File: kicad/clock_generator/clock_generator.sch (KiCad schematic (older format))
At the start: 17 parts, among them J1 DB9_Male, U1 SN74ALVC00, U2 SN74ALVC00, U3 SN74ALVC00, U4 SN74ALVC00

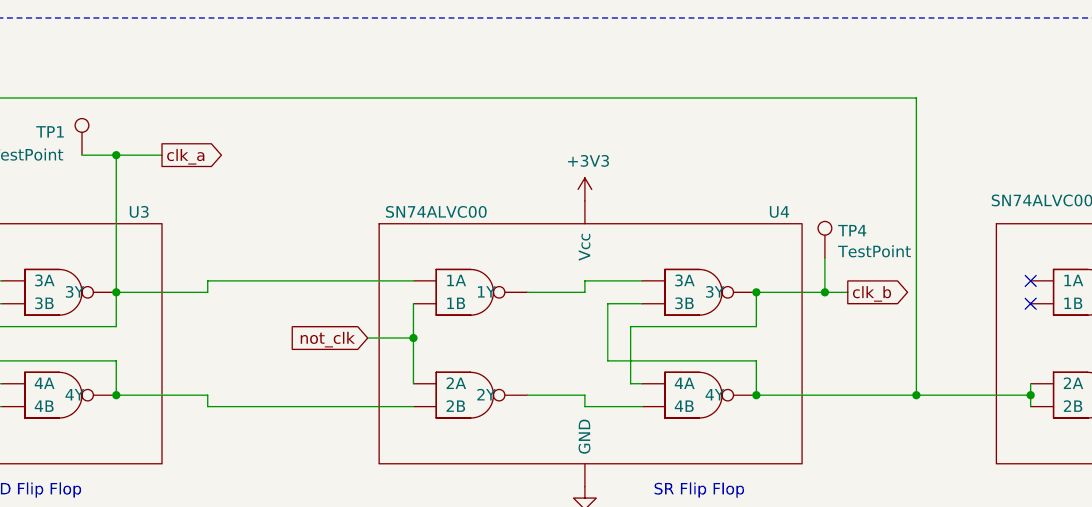
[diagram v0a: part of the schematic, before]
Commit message: Flipped clk A and clk B based on timing plan.
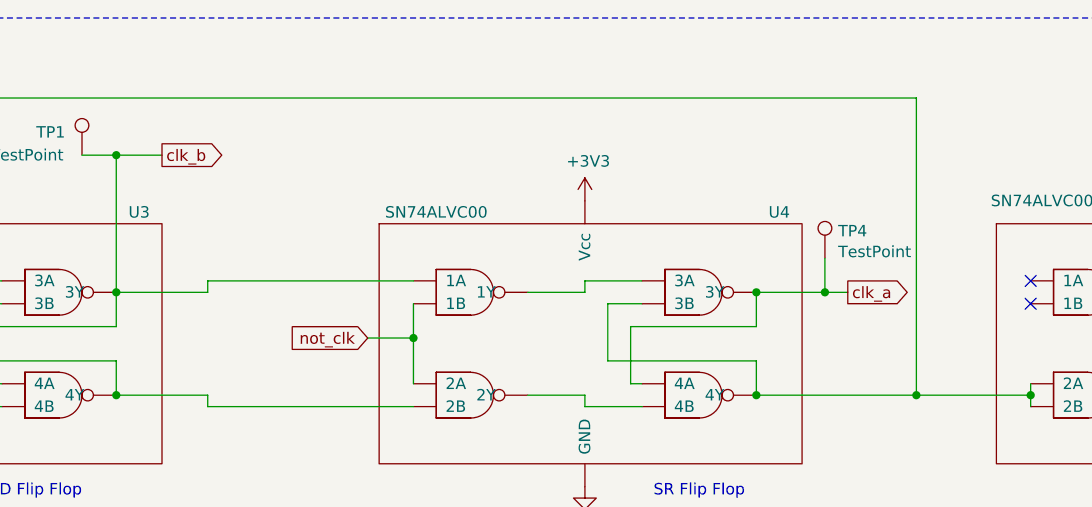
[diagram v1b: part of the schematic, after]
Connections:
- net clk_a: now also TP4.1, U4.12 (4A), U4.8 (3Y); no longer TP1.1, U3.12 (4A), U3.8 (3Y), U4.1 (1A)
- net clk_b: now also TP1.1, U3.12 (4A), U3.8 (3Y), U4.1 (1A); no longer TP4.1, U4.12 (4A), U4.8 (3Y)
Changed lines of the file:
@@
 Connection ~ 3950 2600
 Text GLabel 4150 1550 2    50   Output ~ 0
-clk_a
+clk_b
 Wire Wire Line
 	3950 2150 3950 1550
@@
 	3950 1550 4150 1550
 Text GLabel 7150 2150 2    50   Output ~ 0
-clk_b
+clk_a
 Wire Wire Line
 	3000 5600 3050 5600

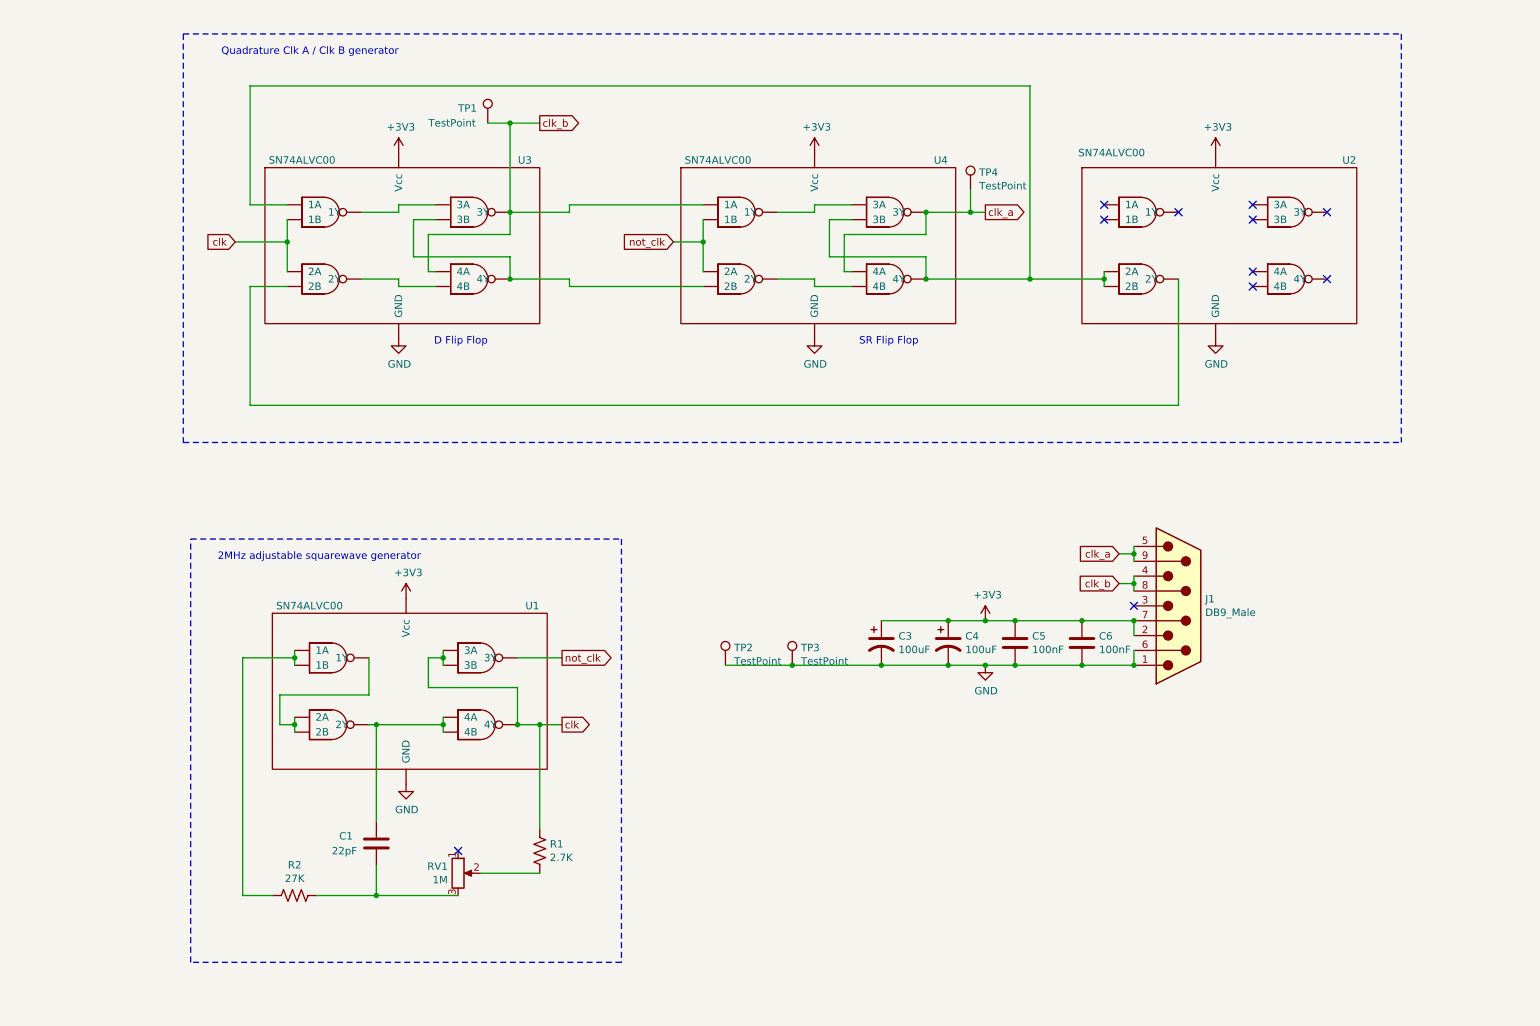
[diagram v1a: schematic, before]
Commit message: Ram (#5)
* Flipped clk A and B based on timing diagram. Added output buffers for clock signals.

* Added clock output enable signal to motherboard debugger. Updated component library.

* Schematic and layout for RAM board complete.

* ALU schematic complete, ready for layout and routing.

* ALU layout, routing complete. Associated motherboard mod. 

* Added Load LED to register and program counter boards.
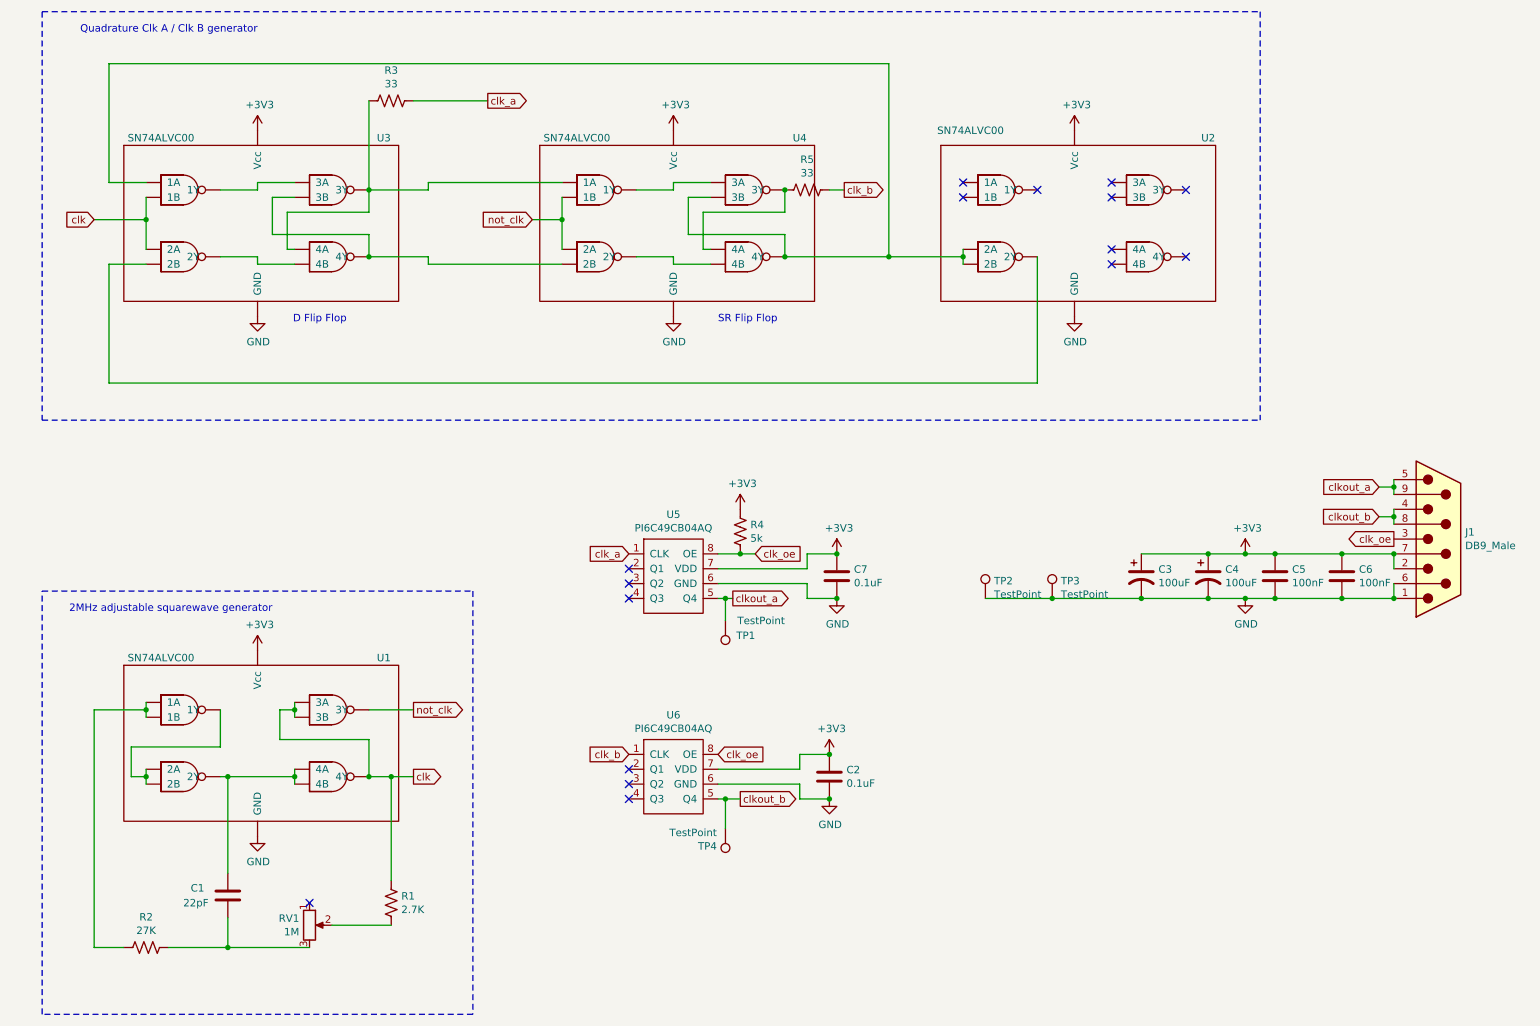
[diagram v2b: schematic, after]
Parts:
- added C2, C7: 0.1uF, Capacitor_SMD:C_1206_3216Metric, symbol Device:C
- added R3, R5: 33, Resistor_SMD:R_1206_3216Metric, symbol Device:R_US
- added R4: 5k, Resistor_SMD:R_1206_3216Metric, symbol Device:R_US
- added U5, U6: PI6C49CB04AQ, Package_SO:SOIC-8_3.9x4.9mm_P1.27mm, symbol NANDIRL_components:PI6C49CB04AQ
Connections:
- net +3V3: now also C2.1, C7.1, R4.2, U5.7 (VDD), U6.7 (VDD)
- net GND: now also C2.2, C7.2, U5.6 (GND), U6.6 (GND)
- net clk_a: now also R3.1, U5.1 (CLK); no longer J1.5, J1.9, TP4.1, U4.12 (4A), U4.8 (3Y)
- net clk_b: now also R5.1, U6.1 (CLK); no longer J1.4, J1.8, TP1.1, U3.12 (4A), U3.8 (3Y), U4.1 (1A)
- net clk_oe: now reaches J1.3
- net clk_oe: now also R4.1, U5.8 (OE), U6.8 (OE)
- new net: R3.2, U3.12 (4A), U3.8 (3Y), U4.1 (1A)
- new net: R5.2, U4.12 (4A), U4.8 (3Y)
- new net clkout_a: J1.5, J1.9, TP1.1, U5.5 (Q4)
- new net clkout_b: J1.4, J1.8, TP4.1, U6.5 (Q4)
- no-connect marks 11 -> 16
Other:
- moved on the sheet: C1, C3, C4, C5, C6, J1, R1, R2, RV1, TP1, TP2, TP3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

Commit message: Readme updates (#6)
* Readme intro section

* Board revisions for manufacturing, add digikey PNs to all, added logo.
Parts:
- C2, C7: Digikey PN (none) -> 399-C1206C104K5RAC7800CT-ND
- J1: footprint Connector_Dsub:DSUB-9_Male_Horizontal_P2.77x2.84mm_EdgePinOffset4.94mm_Housed_MountingHolesOffset7.48mm -> Connector_Dsub:DSUB-9_Male_Horizontal_P2.77x2.84mm_EdgePinOffset7.70mm_Housed_MountingHolesOffset9.12mm; Digikey PN (none) -> AE10968-ND
- R3, R5: Digikey PN (none) -> P33ECT-ND
- R4: Digikey PN (none) -> P5.1KECT-ND
- U1, U2, U3, U4: Digikey PN (none) -> 296-5104-1-ND
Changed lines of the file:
@@
 F 2 "Package_SO:TSSOP-14_4.4x5mm_P0.65mm" H 2250 -200 50  0001 C CNN
 F 3 "" H 2500 1300 50  0001 C CNN
+F 4 "296-5104-1-ND" H 0   0   50  0001 C CNN "Digikey PN"
 	1    2500 1300
 	1    0    0    -1
@@
 F 2 "Package_SO:TSSOP-14_4.4x5mm_P0.65mm" H 2250 3300 50  0001 C CNN
 F 3 "" H 2500 4800 50  0001 C CNN
+F 4 "296-5104-1-ND" H 0   0   50  0001 C CNN "Digikey PN"
 	1    2500 4800
 	1    0    0    -1
@@
 F 2 "Package_SO:TSSOP-14_4.4x5mm_P0.65mm" H 7750 -200 50  0001 C CNN
 F 3 "" H 8000 1300 50  0001 C CNN
+F 4 "296-5104-1-ND" H 0   0   50  0001 C CNN "Digikey PN"
 	1    8000 1300
 	1    0    0    -1
@@
 F 2 "Package_SO:TSSOP-14_4.4x5mm_P0.65mm" H 5050 -200 50  0001 C CNN
 F 3 "" H 5300 1300 50  0001 C CNN
+F 4 "296-5104-1-ND" H 0   0   50  0001 C CNN "Digikey PN"
 	1    5300 1300
 	1    0    0    -1
@@
 F 0 "J1" H 10380 4396 50  0000 L CNN
 F 1 "DB9_Male" H 10380 4305 50  0000 L CNN
-F 2 "Connector_Dsub:DSUB-9_Male_Horizontal_P2.77x2.84mm_EdgePinOffset4.94mm_Housed_MountingHolesOffset7.48mm" H 10200 4350 50  0001 C CNN
+F 2 "Connector_Dsub:DSUB-9_Male_Horizontal_P2.77x2.84mm_EdgePinOffset7.70mm_Housed_MountingHolesOffset9.12mm" H 10200 4350 50  0001 C CNN
 F 3 " ~" H 10200 4350 50  0001 C CNN
+F 4 "AE10968-ND" H 10200 4350 50  0001 C CNN "Digikey PN"
 	1    10200 4350
 	1    0    0    -1
@@
 F 2 "Resistor_SMD:R_1206_3216Metric" V 3190 1390 50  0001 C CNN
 F 3 "~" H 3150 1400 50  0001 C CNN
+F 4 "P33ECT-ND" V 3150 1400 50  0001 C CNN "Digikey PN"
 	1    3150 1400
 	0    1    1    0
@@
 F 2 "Resistor_SMD:R_1206_3216Metric" V 5990 1990 50  0001 C CNN
 F 3 "~" H 5950 2000 50  0001 C CNN
+F 4 "P33ECT-ND" V 5950 2000 50  0001 C CNN "Digikey PN"
 	1    5950 2000
 	0    1    1    0
@@
 F 2 "Capacitor_SMD:C_1206_3216Metric" H 6188 4450 50  0001 C CNN
 F 3 "~" H 6150 4600 50  0001 C CNN
+F 4 "399-C1206C104K5RAC7800CT-ND" H 6150 4600 50  0001 C CNN "Digikey PN"
 	1    6150 4600
 	1    0    0    -1
@@
 F 2 "Capacitor_SMD:C_1206_3216Metric" H 6138 5800 50  0001 C CNN
 F 3 "~" H 6100 5950 50  0001 C CNN
+F 4 "399-C1206C104K5RAC7800CT-ND" H 6100 5950 50  0001 C CNN "Digikey PN"
 	1    6100 5950
 	1    0    0    -1
@@
 F 2 "Resistor_SMD:R_1206_3216Metric" V 5540 4290 50  0001 C CNN
 F 3 "~" H 5500 4300 50  0001 C CNN
+F 4 "P5.1KECT-ND" H 5500 4300 50  0001 C CNN "Digikey PN"
 	1    5500 4300
 	-1   0    0    1
